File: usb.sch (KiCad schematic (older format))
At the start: 25 parts, among them J4 CONN_02X03, U1 LFE5U-45F-6BG381C, U6 FT231XS, Y1 FNETHE025

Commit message: schematics: replace 45F chip with 85F
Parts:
- U1: value LFE5U-45F-6BG381C -> LFE5U-85F-6BG381C; symbol lfe5bg381:LFE5U-45F-6BG381C -> lfe5bg381:LFE5U-85F-6BG381C; MFG_PN LFE5U-45F-6BG381C -> LFE5U-85F-6BG381C
- U1: value LFE5U-45F-6BG381C -> LFE5U-85F-6BG381C; symbol lfe5bg381:LFE5U-45F-6BG381C -> lfe5bg381:LFE5U-85F-6BG381C; Distributor1_PN 842-LFE5U45F6BG381C -> 842-LFE5U85F6BG381C; MFG_PN LFE5U-45F-6BG381C -> LFE5U-85F-6BG381C
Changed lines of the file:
@@
 Short circuit R56\nfor chip rev A,B,C\nworkaround in \nTN140_FT231X Errata
 $Comp
-L lfe5bg381:LFE5U-45F-6BG381C U1
+L lfe5bg381:LFE5U-85F-6BG381C U1
 U 5 1 5A079A7A
 P 9400 2050
@@
 AR Path="/58D6BF46/5A079A7A" Ref="U1"  Part="5"
 F 0 "U1" H 9400 3000 60  0000 C CNN
-F 1 "LFE5U-45F-6BG381C" H 9400 2900 60  0000 C CNN
+F 1 "LFE5U-85F-6BG381C" H 9400 2900 60  0000 C CNN
 F 2 "lfe5bg381:BGA-381_pitch0.8mm_dia0.4mm" H 8350 3000 60  0001 C CNN
 F 3 "http://www.latticesemi.com/~/media/LatticeSemi/Documents/DataSheets/ECP5/FPGA-DS-02012.pdf" H 8350 3000 60  0001 C CNN
-F 4 "LFE5U-45F-6BG381C" H 9400 2050 60  0001 C CNN "MFG_PN"
+F 4 "LFE5U-85F-6BG381C" H 9400 2050 60  0001 C CNN "MFG_PN"
 F 5 "www.mouser.com" H 9400 2050 60  0001 C CNN "Distributor1_URL"
 	5    9400 2050
@@
 $EndComp
 $Comp
-L lfe5bg381:LFE5U-45F-6BG381C U1
+L lfe5bg381:LFE5U-85F-6BG381C U1
 U 10 1 5A07A05D
 P 8600 3950
@@
 AR Path="/58D6BF46/5A07A05D" Ref="U1"  Part="10"
 F 0 "U1" H 8550 4350 60  0000 C CNN
-F 1 "LFE5U-45F-6BG381C" H 8550 4250 60  0000 C CNN
+F 1 "LFE5U-85F-6BG381C" H 8550 4250 60  0000 C CNN
 F 2 "lfe5bg381:BGA-381_pitch0.8mm_dia0.4mm" H 7550 4900 60  0001 C CNN
 F 3 "http://www.latticesemi.com/~/media/LatticeSemi/Documents/DataSheets/ECP5/FPGA-DS-02012.pdf" H 7550 4900 60  0001 C CNN
-F 4 "LFE5U-45F-6BG381C" H 8600 3950 60  0001 C CNN "MFG_PN"
+F 4 "LFE5U-85F-6BG381C" H 8600 3950 60  0001 C CNN "MFG_PN"
 F 5 "www.mouser.com" H 8600 3950 60  0001 C CNN "Distributor1_URL"
-F 6 "842-LFE5U45F6BG381C" H 8600 3950 60  0001 C CNN "Distributor1_PN"
+F 6 "842-LFE5U85F6BG381C" H 8600 3950 60  0001 C CNN "Distributor1_PN"
 	10   8600 3950
 	-1   0    0    -1

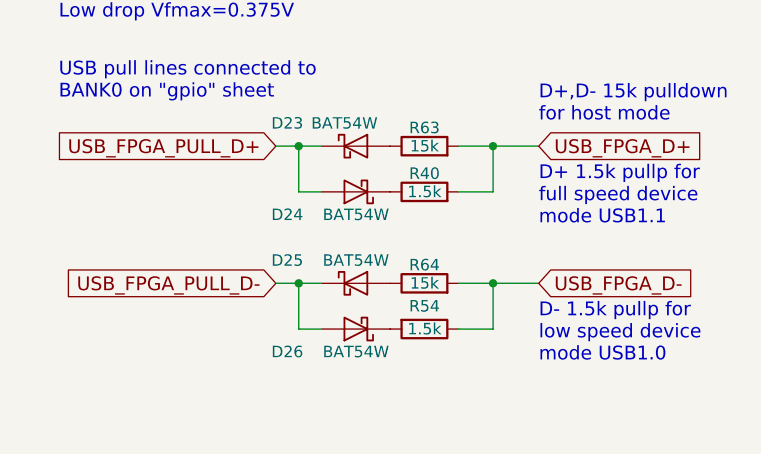
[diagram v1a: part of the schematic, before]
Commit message: schematics: BAT54 specified PN
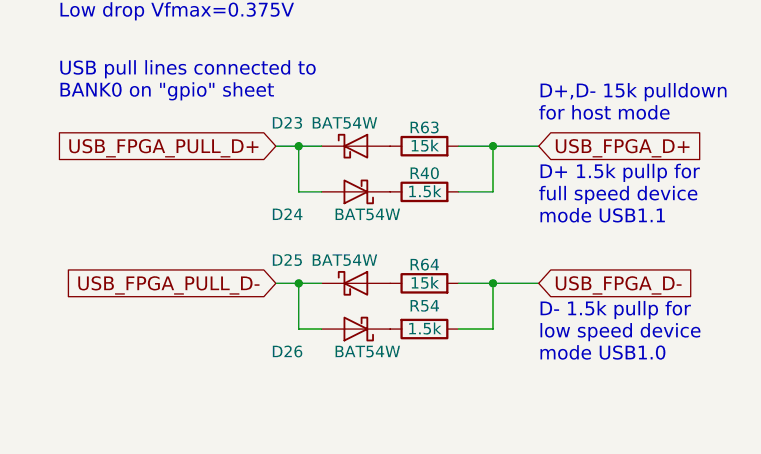
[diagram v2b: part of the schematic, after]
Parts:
- D23, D24, D25, D26: Distributor1_PN (none) -> 621-BAT54WSQ-7-F; Distributor1_URL (none) -> www.mouser.com; MFG_PN (none) -> BAT54WSQ-7-F; MFG_URL (none) -> www.diodes.com
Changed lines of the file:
@@
 F 1 "BAT54W" H 1900 4750 50  0000 C CNN
 F 2 "Diodes_SMD:D_SOD-323_HandSoldering" V 1950 4650 50  0001 C CNN
-F 3 "" V 1950 4650 50  0001 C CNN
+F 3 "https://www.diodes.com/assets/Datasheets/ds30065.pdf" V 1950 4650 50  0001 C CNN
+F 4 "www.diodes.com" H 1950 4650 50  0001 C CNN "MFG_URL"
+F 5 "BAT54WSQ-7-F" H 1950 4650 50  0001 C CNN "MFG_PN"
+F 6 "www.mouser.com" H 1950 4650 50  0001 C CNN "Distributor1_URL"
+F 7 "621-BAT54WSQ-7-F" H 1950 4650 50  0001 C CNN "Distributor1_PN"
 	1    1950 4650
 	1    0    0    -1
-$EndComp
-$Comp
-L ulx3s-rescue:D_Schottky D24
-U 1 1 5A7212CC
-P 1950 4850
-F 0 "D24" H 2250 4950 50  0000 C CNN
-F 1 "BAT54W" H 1950 4950 50  0000 C CNN
-F 2 "Diodes_SMD:D_SOD-323_HandSoldering" V 1950 4850 50  0001 C CNN
-F 3 "" V 1950 4850 50  0001 C CNN
-	1    1950 4850
-	-1   0    0    1
-$EndComp
-$Comp
-L ulx3s-rescue:D_Schottky D25
-U 1 1 5A72158A
-P 1950 5250
-F 0 "D25" H 1650 5350 50  0000 C CNN
-F 1 "BAT54W" H 1950 4950 50  0000 C CNN
-F 2 "Diodes_SMD:D_SOD-323_HandSoldering" V 1950 5250 50  0001 C CNN
-F 3 "" V 1950 5250 50  0001 C CNN
-	1    1950 5250
-	1    0    0    -1
-$EndComp
-$Comp
-L ulx3s-rescue:D_Schottky D26
-U 1 1 5A7218C4
-P 1950 5450
-F 0 "D26" H 2250 5550 50  0000 C CNN
-F 1 "BAT54W" H 1950 5150 50  0000 C CNN
-F 2 "Diodes_SMD:D_SOD-323_HandSoldering" V 1950 5450 50  0001 C CNN
-F 3 "" V 1950 5450 50  0001 C CNN
-	1    1950 5450
-	-1   0    0    1
 $EndComp
 Wire Wire Line
@@
 Wire Wire Line
 	1700 5250 1800 5250
+$Comp
+L ulx3s-rescue:D_Schottky D25
+U 1 1 5AF760EE
+P 1950 5250
+F 0 "D25" H 1650 5350 50  0000 C CNN
+F 1 "BAT54W" H 1900 5350 50  0000 C CNN
+F 2 "Diodes_SMD:D_SOD-323_HandSoldering" V 1950 5250 50  0001 C CNN
+F 3 "https://www.diodes.com/assets/Datasheets/ds30065.pdf" V 1950 5250 50  0001 C CNN
+F 4 "www.diodes.com" H 1950 5250 50  0001 C CNN "MFG_URL"
+F 5 "BAT54WSQ-7-F" H 1950 5250 50  0001 C CNN "MFG_PN"
+F 6 "www.mouser.com" H 1950 5250 50  0001 C CNN "Distributor1_URL"
+F 7 "621-BAT54WSQ-7-F" H 1950 5250 50  0001 C CNN "Distributor1_PN"
+	1    1950 5250
+	1    0    0    -1
+$EndComp
+$Comp
+L ulx3s-rescue:D_Schottky D24
+U 1 1 5AF79ABE
+P 1950 4850
+F 0 "D24" H 2250 4950 50  0000 C CNN
+F 1 "BAT54W" H 1900 4950 50  0000 C CNN
+F 2 "Diodes_SMD:D_SOD-323_HandSoldering" V 1950 4850 50  0001 C CNN
+F 3 "https://www.diodes.com/assets/Datasheets/ds30065.pdf" V 1950 4850 50  0001 C CNN
+F 4 "www.diodes.com" H 1950 4850 50  0001 C CNN "MFG_URL"
+F 5 "BAT54WSQ-7-F" H 1950 4850 50  0001 C CNN "MFG_PN"
+F 6 "www.mouser.com" H 1950 4850 50  0001 C CNN "Distributor1_URL"
+F 7 "621-BAT54WSQ-7-F" H 1950 4850 50  0001 C CNN "Distributor1_PN"
+	1    1950 4850
+	-1   0    0    1
+$EndComp
+$Comp
+L ulx3s-rescue:D_Schottky D26
+U 1 1 5AF7B2B2
+P 1950 5450
+F 0 "D26" H 2250 5550 50  0000 C CNN
+F 1 "BAT54W" H 1900 5550 50  0000 C CNN
+F 2 "Diodes_SMD:D_SOD-323_HandSoldering" V 1950 5450 50  0001 C CNN
+F 3 "https://www.diodes.com/assets/Datasheets/ds30065.pdf" V 1950 5450 50  0001 C CNN
+F 4 "www.diodes.com" H 1950 5450 50  0001 C CNN "MFG_URL"
+F 5 "BAT54WSQ-7-F" H 1950 5450 50  0001 C CNN "MFG_PN"
+F 6 "www.mouser.com" H 1950 5450 50  0001 C CNN "Distributor1_URL"
+F 7 "621-BAT54WSQ-7-F" H 1950 5450 50  0001 C CNN "Distributor1_PN"
+	1    1950 5450
+	-1   0    0    1
+$EndComp
 $EndSCHEMATC

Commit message: schematics: hopefully getting rid of all references to micro-gpdi-d
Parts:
- AE1: symbol ulx3s-rescue:Antenna -> Device:Antenna
- J4: symbol micro-hdmi-d:CONN_02X03 -> Connector_Generic:Conn_02x03_Odd_Even
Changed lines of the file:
@@
 CLK_25MHz
 $Comp
-L micro-hdmi-d:CONN_02X03 J4
+L Connector_Generic:Conn_02x03_Odd_Even J4
 U 1 1 591E0E6A
-P 9400 5000
-F 0 "J4" H 9400 5200 50  0000 C CNN
-F 1 "CONN_02X03" H 9400 4800 50  0000 C CNN
-F 2 "Socket_Strips:Socket_Strip_Straight_2x03" H 9400 3800 50  0001 C CNN
-F 3 "" H 9400 3800 50  0000 C CNN
-F 4 "Do not install" H 9400 5000 60  0001 C CNN "Note"
-	1    9400 5000
+P 9350 5000
+F 0 "J4" H 9350 5200 50  0000 C CNN
+F 1 "CONN_02X03" H 9350 4800 50  0000 C CNN
+F 2 "Socket_Strips:Socket_Strip_Straight_2x03" H 9350 3800 50  0001 C CNN
+F 3 "" H 9350 3800 50  0000 C CNN
+F 4 "Do not install" H 9350 5000 60  0001 C CNN "Note"
+	1    9350 5000
 	1    0    0    -1
 $EndComp
@@
 WIFI_GPIO16
 $Comp
-L ulx3s-rescue:Antenna AE1
+L Device:Antenna AE1
 U 1 1 59C3AE47
 P 10950 1350

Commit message: schematics: updating new diodes symbols
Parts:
- D20, D21, D23, D24, D25, D26: footprint Diodes_SMD:D_SOD-323_HandSoldering -> Diode_SMD:D_SOD-323_HandSoldering
- D8, D9: footprint Diodes_SMD:D_SMA_Handsoldering -> Diode_SMD:D_SMA_Handsoldering
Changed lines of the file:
@@
 F 0 "D8" H 2350 1650 50  0000 L CNN
 F 1 "STPS2L30AF" H 1800 1650 50  0000 L CNN
-F 2 "Diodes_SMD:D_SMA_Handsoldering" V 2300 1700 60  0001 C CNN
+F 2 "Diode_SMD:D_SMA_Handsoldering" V 2300 1700 60  0001 C CNN
 F 3 "" V 2300 1700 60  0000 C CNN
 F 4 "STPS2L30AF" H 2300 1700 60  0001 C CNN "MFG_PN"
@@
 F 0 "D9" H 2450 2700 50  0000 L CNN
 F 1 "STPS2L30AF" H 2650 2700 50  0000 L CNN
-F 2 "Diodes_SMD:D_SMA_Handsoldering" V 2600 2650 60  0001 C CNN
+F 2 "Diode_SMD:D_SMA_Handsoldering" V 2600 2650 60  0001 C CNN
 F 3 "" V 2600 2650 60  0000 C CNN
 F 4 "STPS2L30AF" H 2600 2650 60  0001 C CNN "MFG_PN"
@@
 F 0 "D20" H 2800 2900 50  0000 C CNN
 F 1 "3.6V" H 2600 2910 50  0000 C CNN
-F 2 "Diodes_SMD:D_SOD-323_HandSoldering" V 2600 3000 50  0001 C CNN
+F 2 "Diode_SMD:D_SOD-323_HandSoldering" V 2600 3000 50  0001 C CNN
 F 3 "http://www.taiwansemi.com/products/datasheet/BZT52C2V4S%20SERIES_H1709.pdf" V 2600 3000 50  0001 C CNN
 F 4 "http://www.taiwansemi.com/en" H 2600 3000 60  0001 C CNN "MFG_URL"
@@
 F 0 "D21" H 2900 3100 50  0000 C CNN
 F 1 "3.6V" H 2700 3100 50  0000 C CNN
-F 2 "Diodes_SMD:D_SOD-323_HandSoldering" V 2700 3000 50  0001 C CNN
+F 2 "Diode_SMD:D_SOD-323_HandSoldering" V 2700 3000 50  0001 C CNN
 F 3 "http://www.taiwansemi.com/products/datasheet/BZT52C2V4S%20SERIES_H1709.pdf" V 2700 3000 50  0001 C CNN
 F 4 "http://www.taiwansemi.com/en" H 2700 3000 60  0001 C CNN "MFG_URL"
@@
 F 0 "D23" H 1650 4750 50  0000 C CNN
 F 1 "BAT54W" H 1900 4750 50  0000 C CNN
-F 2 "Diodes_SMD:D_SOD-323_HandSoldering" V 1950 4650 50  0001 C CNN
+F 2 "Diode_SMD:D_SOD-323_HandSoldering" V 1950 4650 50  0001 C CNN
 F 3 "https://www.diodes.com/assets/Datasheets/ds30065.pdf" V 1950 4650 50  0001 C CNN
 F 4 "www.diodes.com" H 1950 4650 50  0001 C CNN "MFG_URL"
@@
 F 0 "D25" H 1650 5350 50  0000 C CNN
 F 1 "BAT54W" H 1900 5350 50  0000 C CNN
-F 2 "Diodes_SMD:D_SOD-323_HandSoldering" V 1950 5250 50  0001 C CNN
+F 2 "Diode_SMD:D_SOD-323_HandSoldering" V 1950 5250 50  0001 C CNN
 F 3 "https://www.diodes.com/assets/Datasheets/ds30065.pdf" V 1950 5250 50  0001 C CNN
 F 4 "www.diodes.com" H 1950 5250 50  0001 C CNN "MFG_URL"
@@
 F 0 "D24" H 2250 4950 50  0000 C CNN
 F 1 "BAT54W" H 1900 4950 50  0000 C CNN
-F 2 "Diodes_SMD:D_SOD-323_HandSoldering" V 1950 4850 50  0001 C CNN
+F 2 "Diode_SMD:D_SOD-323_HandSoldering" V 1950 4850 50  0001 C CNN
 F 3 "https://www.diodes.com/assets/Datasheets/ds30065.pdf" V 1950 4850 50  0001 C CNN
 F 4 "www.diodes.com" H 1950 4850 50  0001 C CNN "MFG_URL"
@@
 F 0 "D26" H 2250 5550 50  0000 C CNN
 F 1 "BAT54W" H 1900 5550 50  0000 C CNN
-F 2 "Diodes_SMD:D_SOD-323_HandSoldering" V 1950 5450 50  0001 C CNN
+F 2 "Diode_SMD:D_SOD-323_HandSoldering" V 1950 5450 50  0001 C CNN
 F 3 "https://www.diodes.com/assets/Datasheets/ds30065.pdf" V 1950 5450 50  0001 C CNN
 F 4 "www.diodes.com" H 1950 5450 50  0001 C CNN "MFG_URL"

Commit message: schematics: antenna as test point
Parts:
- AE1: footprint Pin_Headers:Pin_Header_Straight_1x03_Pitch2.54mm -> TestPoint:TestPoint_Pad_D1.0mm
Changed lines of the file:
@@
 F 0 "AE1" H 10875 1425 50  0000 R CNN
 F 1 "433MHz" H 10875 1350 50  0000 R CNN
-F 2 "Pin_Headers:Pin_Header_Straight_1x03_Pitch2.54mm" H 10950 1350 50  0001 C CNN
+F 2 "TestPoint:TestPoint_Pad_D1.0mm" H 10950 1350 50  0001 C CNN
 F 3 "" H 10950 1350 50  0001 C CNN
 F 4 "Do not install" H 10950 1350 60  0001 C CNN "Note"

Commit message: schematics: updating resistor footprints
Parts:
- R40, R63, R64: footprint Resistors_SMD:R_0603 -> Resistor_SMD:R_0603_1608Metric_Pad0.84x1.00mm_HandSolder
- R49, R50, R52, R53, R56: footprint Resistors_SMD:R_0603_HandSoldering -> Resistor_SMD:R_0603_1608Metric
- R54: footprint Resistors_SMD:R_0603 -> Resistor_SMD:R_0603_1608Metric
- R9: footprint Resistors_SMD:R_0603_HandSoldering -> Resistor_SMD:R_0603_1608Metric_Pad0.84x1.00mm_HandSolder
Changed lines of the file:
@@
 F 0 "R9" V 4780 3600 50  0000 C CNN
 F 1 "15k" V 4700 3600 50  0000 C CNN
-F 2 "Resistors_SMD:R_0603_HandSoldering" V 4630 3600 50  0001 C CNN
+F 2 "Resistor_SMD:R_0603_1608Metric_Pad0.84x1.00mm_HandSolder" V 4630 3600 50  0001 C CNN
 F 3 "" H 4700 3600 50  0000 C CNN
 	1    4700 3600
@@
 F 0 "R40" V 2330 4850 50  0000 C CNN
 F 1 "1.5k" V 2250 4850 50  0000 C CNN
-F 2 "Resistors_SMD:R_0603" V 2180 4850 50  0001 C CNN
+F 2 "Resistor_SMD:R_0603_1608Metric_Pad0.84x1.00mm_HandSolder" V 2180 4850 50  0001 C CNN
 F 3 "" H 2250 4850 50  0000 C CNN
 	1    2250 4850
@@
 F 0 "R49" V 2250 2000 50  0000 C CNN
 F 1 "27" V 2300 1800 50  0000 C CNN
-F 2 "Resistors_SMD:R_0603_HandSoldering" V 2230 1800 50  0001 C CNN
+F 2 "Resistor_SMD:R_0603_1608Metric" V 2230 1800 50  0001 C CNN
 F 3 "" H 2300 1800 50  0000 C CNN
 	1    2300 1800
@@
 F 0 "R50" V 2250 2100 50  0000 C CNN
 F 1 "27" V 2300 1900 50  0000 C CNN
-F 2 "Resistors_SMD:R_0603_HandSoldering" V 2230 1900 50  0001 C CNN
+F 2 "Resistor_SMD:R_0603_1608Metric" V 2230 1900 50  0001 C CNN
 F 3 "" H 2300 1900 50  0000 C CNN
 	1    2300 1900
@@
 F 0 "R52" V 2200 2950 50  0000 C CNN
 F 1 "27" V 2250 2750 50  0000 C CNN
-F 2 "Resistors_SMD:R_0603_HandSoldering" V 2180 2750 50  0001 C CNN
+F 2 "Resistor_SMD:R_0603_1608Metric" V 2180 2750 50  0001 C CNN
 F 3 "" H 2250 2750 50  0000 C CNN
 	1    2250 2750
@@
 F 0 "R53" V 2200 3050 50  0000 C CNN
 F 1 "27" V 2250 2850 50  0000 C CNN
-F 2 "Resistors_SMD:R_0603_HandSoldering" V 2180 2850 50  0001 C CNN
+F 2 "Resistor_SMD:R_0603_1608Metric" V 2180 2850 50  0001 C CNN
 F 3 "" H 2250 2850 50  0000 C CNN
 	1    2250 2850
@@
 F 0 "R54" V 2150 5450 50  0000 C CNN
 F 1 "1.5k" V 2250 5450 50  0000 C CNN
-F 2 "Resistors_SMD:R_0603" V 2180 5450 50  0001 C CNN
+F 2 "Resistor_SMD:R_0603_1608Metric" V 2180 5450 50  0001 C CNN
 F 3 "" H 2250 5450 50  0000 C CNN
 	1    2250 5450
@@
 F 0 "R56" V 6530 4250 50  0000 C CNN
 F 1 "0" V 6450 4250 50  0000 C CNN
-F 2 "Resistors_SMD:R_0603_HandSoldering" V 6380 4250 50  0001 C CNN
+F 2 "Resistor_SMD:R_0603_1608Metric" V 6380 4250 50  0001 C CNN
 F 3 "" H 6450 4250 50  0000 C CNN
 F 4 "Do not install" H 6450 4250 60  0001 C CNN "Note"
@@
 F 0 "R63" V 2330 4650 50  0000 C CNN
 F 1 "15k" V 2250 4650 50  0000 C CNN
-F 2 "Resistors_SMD:R_0603" V 2180 4650 50  0001 C CNN
+F 2 "Resistor_SMD:R_0603_1608Metric_Pad0.84x1.00mm_HandSolder" V 2180 4650 50  0001 C CNN
 F 3 "" H 2250 4650 50  0000 C CNN
 	1    2250 4650
@@
 F 0 "R64" V 2330 5250 50  0000 C CNN
 F 1 "15k" V 2250 5250 50  0000 C CNN
-F 2 "Resistors_SMD:R_0603" V 2180 5250 50  0001 C CNN
+F 2 "Resistor_SMD:R_0603_1608Metric_Pad0.84x1.00mm_HandSolder" V 2180 5250 50  0001 C CNN
 F 3 "" H 2250 5250 50  0000 C CNN
 	1    2250 5250

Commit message: schematics: set part numbers for most resistors
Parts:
- R40: footprint Resistor_SMD:R_0603_1608Metric_Pad0.84x1.00mm_HandSolder -> Resistor_SMD:R_0603_1608Metric; MFG_PN (none) -> RC0603FR-071K5L
- R49, R50, R52, R53: MFG_PN (none) -> AC0603JR-0727RL
- R54: MFG_PN (none) -> RC0603FR-071K5L
- R63, R64, R9: MFG_PN (none) -> AC0603FR-1015KL
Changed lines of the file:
@@
 F 2 "Resistor_SMD:R_0603_1608Metric_Pad0.84x1.00mm_HandSolder" V 4630 3600 50  0001 C CNN
 F 3 "" H 4700 3600 50  0000 C CNN
+F 4 "AC0603FR-1015KL" V 4700 3600 50  0001 C CNN "MFG_PN"
 	1    4700 3600
 	0    1    1    0
@@
 F 0 "R40" V 2330 4850 50  0000 C CNN
 F 1 "1.5k" V 2250 4850 50  0000 C CNN
-F 2 "Resistor_SMD:R_0603_1608Metric_Pad0.84x1.00mm_HandSolder" V 2180 4850 50  0001 C CNN
+F 2 "Resistor_SMD:R_0603_1608Metric" V 2180 4850 50  0001 C CNN
 F 3 "" H 2250 4850 50  0000 C CNN
+F 4 "RC0603FR-071K5L" V 2250 4850 50  0001 C CNN "MFG_PN"
 	1    2250 4850
 	0    -1   -1   0
@@
 F 2 "Resistor_SMD:R_0603_1608Metric" V 2230 1800 50  0001 C CNN
 F 3 "" H 2300 1800 50  0000 C CNN
+F 4 "AC0603JR-0727RL" V 2300 1800 50  0001 C CNN "MFG_PN"
 	1    2300 1800
 	0    1    1    0
@@
 F 2 "Resistor_SMD:R_0603_1608Metric" V 2230 1900 50  0001 C CNN
 F 3 "" H 2300 1900 50  0000 C CNN
+F 4 "AC0603JR-0727RL" V 2300 1900 50  0001 C CNN "MFG_PN"
 	1    2300 1900
 	0    1    1    0
@@
 F 2 "Resistor_SMD:R_0603_1608Metric" V 2180 2750 50  0001 C CNN
 F 3 "" H 2250 2750 50  0000 C CNN
+F 4 "AC0603JR-0727RL" V 2250 2750 50  0001 C CNN "MFG_PN"
 	1    2250 2750
 	0    1    1    0
@@
 F 2 "Resistor_SMD:R_0603_1608Metric" V 2180 2850 50  0001 C CNN
 F 3 "" H 2250 2850 50  0000 C CNN
+F 4 "AC0603JR-0727RL" V 2250 2850 50  0001 C CNN "MFG_PN"
 	1    2250 2850
 	0    1    1    0
@@
 F 2 "Resistor_SMD:R_0603_1608Metric" V 2180 5450 50  0001 C CNN
 F 3 "" H 2250 5450 50  0000 C CNN
+F 4 "RC0603FR-071K5L" V 2250 5450 50  0001 C CNN "MFG_PN"
 	1    2250 5450
 	0    1    1    0
@@
 F 2 "Resistor_SMD:R_0603_1608Metric_Pad0.84x1.00mm_HandSolder" V 2180 4650 50  0001 C CNN
 F 3 "" H 2250 4650 50  0000 C CNN
+F 4 "AC0603FR-1015KL" V 2250 4650 50  0001 C CNN "MFG_PN"
 	1    2250 4650
 	0    -1   -1   0
@@
 F 2 "Resistor_SMD:R_0603_1608Metric_Pad0.84x1.00mm_HandSolder" V 2180 5250 50  0001 C CNN
 F 3 "" H 2250 5250 50  0000 C CNN
+F 4 "AC0603FR-1015KL" V 2250 5250 50  0001 C CNN "MFG_PN"
 	1    2250 5250
 	0    -1   -1   0

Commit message: schematics: changing old rescue symbols with new from kicad 5 library
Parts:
- D20, D21: symbol ulx3s-rescue:D_Zener_Small_ALT -> Device:D_Zener_Small_ALT
- D23, D24, D25, D26: symbol ulx3s-rescue:D_Schottky -> Device:D_Schottky
- D8, D9: symbol ulx3s-rescue:D_Schottky_Small -> Device:D_Schottky_Small
- R40, R49, R50, R52, R53, R54, R56, R63, R64, R9: symbol ulx3s-rescue:R -> Device:R
- Y1: symbol ulx3s-rescue:Crystal_GND24 -> Device:Crystal_GND24
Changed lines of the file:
@@
 $EndDescr
 $Comp
-L ulx3s-rescue:D_Schottky_Small D8
+L Device:D_Schottky_Small D8
 U 1 1 58D6C83A
 P 2300 1700
@@
 $EndComp
 $Comp
-L ulx3s-rescue:D_Schottky_Small D9
+L Device:D_Schottky_Small D9
 U 1 1 58D6C83C
 P 2600 2650
@@
 	4850 3400 4950 3400
 $Comp
-L ulx3s-rescue:R R9
+L Device:R R9
 U 1 1 58EB9CB5
 P 4700 3600
@@
 warning:\nULX3S has different pinout\nfor simpler PCB routing and\nbecause FT230X has weak CTS\ndrive capability. (Undocumented,\nFLEAfpga mail from 13-Nov-2015)\nULX2S pinout was:\nTCK = DSR\nTMS = RI\nTDI = CTS\nTDO = DCD\n
 $Comp
-L ulx3s-rescue:R R40
+L Device:R R40
 U 1 1 591C69FB
 P 2250 4850
@@
 	8700 4900 9150 4900
 $Comp
-L ulx3s-rescue:R R49
+L Device:R R49
 U 1 1 59274246
 P 2300 1800
@@
 $EndComp
 $Comp
-L ulx3s-rescue:R R50
+L Device:R R50
 U 1 1 592743C8
 P 2300 1900
@@
 USB_FPGA connected to\nBANK1 on "gpdi" sheet and\nBANK2 on "ram" sheet
 $Comp
-L ulx3s-rescue:R R52
+L Device:R R52
 U 1 1 59C0F7B0
 P 2250 2750
@@
 $EndComp
 $Comp
-L ulx3s-rescue:R R53
+L Device:R R53
 U 1 1 59C0F7B6
 P 2250 2850
@@
 FPD+
 $Comp
-L ulx3s-rescue:D_Zener_Small_ALT D20
+L Device:D_Zener_Small_ALT D20
 U 1 1 59C133D8
 P 2600 3000
@@
 $EndComp
 $Comp
-L ulx3s-rescue:D_Zener_Small_ALT D21
+L Device:D_Zener_Small_ALT D21
 U 1 1 59C134C9
 P 2700 3000
@@
 D8,D9: Schottky 2A/30V \nLow drop Vfmax=0.375V
 $Comp
-L ulx3s-rescue:R R54
+L Device:R R54
 U 1 1 59D562D0
 P 2250 5450
@@
 FTDI_TXDEN
 $Comp
-L ulx3s-rescue:R R56
+L Device:R R56
 U 1 1 59DFFFBE
 P 6450 4250
@@
 $EndComp
 $Comp
-L ulx3s-rescue:Crystal_GND24 Y1
+L Device:Crystal_GND24 Y1
 U 1 1 5A079883
 P 5450 1450
@@
 USB_FPGA_PULL_D-
 $Comp
-L ulx3s-rescue:R R63
+L Device:R R63
 U 1 1 5A71E38F
 P 2250 4650
@@
 $EndComp
 $Comp
-L ulx3s-rescue:R R64
+L Device:R R64
 U 1 1 5A71E566
 P 2250 5250
@@
 USB pull lines connected to\nBANK0 on "gpio" sheet
 $Comp
-L ulx3s-rescue:D_Schottky D23
+L Device:D_Schottky D23
 U 1 1 5A720D44
 P 1950 4650
@@
 	1700 5250 1800 5250
 $Comp
-L ulx3s-rescue:D_Schottky D25
+L Device:D_Schottky D25
 U 1 1 5AF760EE
 P 1950 5250
@@
 $EndComp
 $Comp
-L ulx3s-rescue:D_Schottky D24
+L Device:D_Schottky D24
 U 1 1 5AF79ABE
 P 1950 4850
@@
 $EndComp
 $Comp
-L ulx3s-rescue:D_Schottky D26
+L Device:D_Schottky D26
 U 1 1 5AF7B2B2
 P 1950 5450
